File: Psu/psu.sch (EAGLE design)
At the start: 34 parts, among them Q1 FDPF18N50T, Q2 FDPF18N50T, Q3 FDPF18N50T, Q4 FDPF18N50T, X1 MOUNT-PAD2.0, X2 MOUNT-PAD2.0, X3 MOUNT-PAD2.0, X4 MOUNT-PAD2.0, X5 MOUNT-PAD2.0

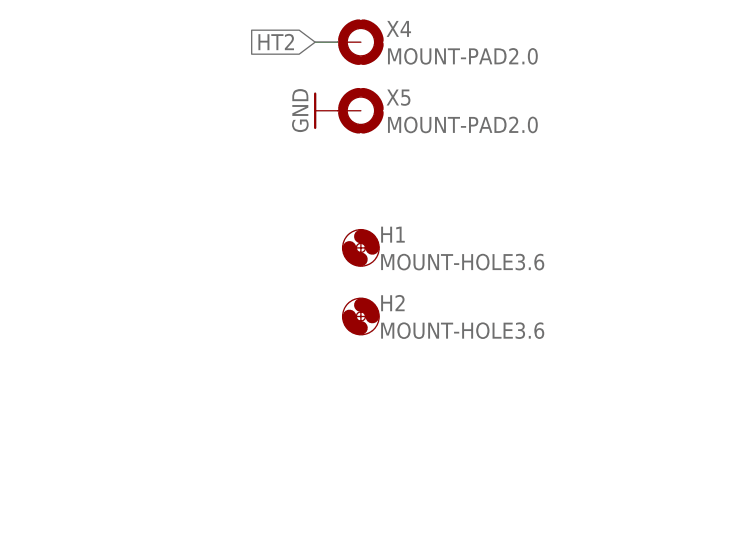
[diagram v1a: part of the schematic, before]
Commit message: More mounting holes
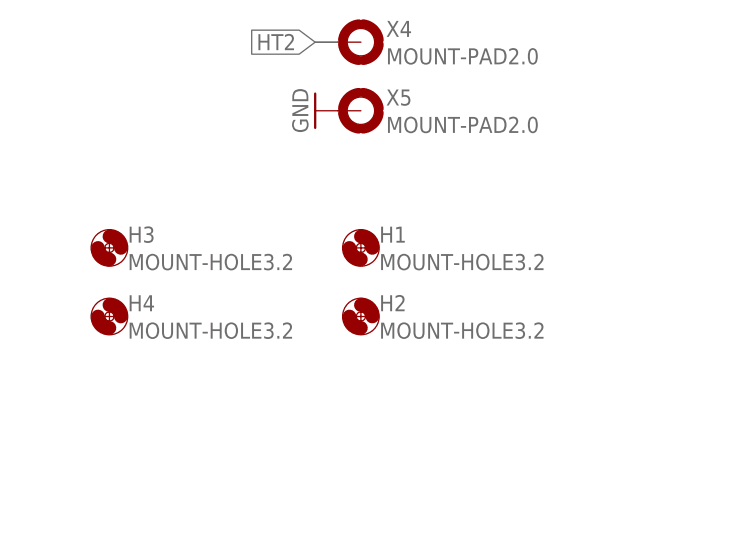
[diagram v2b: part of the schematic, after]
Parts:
- added H3, H4: MOUNT-HOLE3.2, holes:MOUNT-HOLE3.2
- H1, H2: value MOUNT-HOLE3.6 -> MOUNT-HOLE3.2; device holes:MOUNT-HOLE3.6 -> holes:MOUNT-HOLE3.2
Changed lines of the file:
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@@
 <part name="GND2" library="SparkFun-Aesthetics" deviceset="GND" device=""/>
 <part name="LOGO1" library="my" deviceset="LOGO-MANTIS" device=""/>
-<part name="H1" library="holes" deviceset="MOUNT-HOLE" device="3.6"/>
-<part name="H2" library="holes" deviceset="MOUNT-HOLE" device="3.6"/>
+<part name="H1" library="holes" deviceset="MOUNT-HOLE" device="3.2" value="MOUNT-HOLE3.2"/>
+<part name="H2" library="holes" deviceset="MOUNT-HOLE" device="3.2" value="MOUNT-HOLE3.2"/>
+<part name="H3" library="holes" deviceset="MOUNT-HOLE" device="3.2" value="MOUNT-HOLE3.2"/>
+<part name="H4" library="holes" deviceset="MOUNT-HOLE" device="3.2" value="MOUNT-HOLE3.2"/>
 </parts>
 <sheets>
@@
 <instance part="H1" gate="G$1" x="60.96" y="35.56"/>
 <instance part="H2" gate="G$1" x="60.96" y="27.94"/>
+<instance part="H3" gate="G$1" x="33.02" y="35.56"/>
+<instance part="H4" gate="G$1" x="33.02" y="27.94"/>
 </instances>
 <busses>
